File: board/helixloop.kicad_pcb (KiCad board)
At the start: 2 copper layers, 139.8 x 139.8 mm, 357 parts

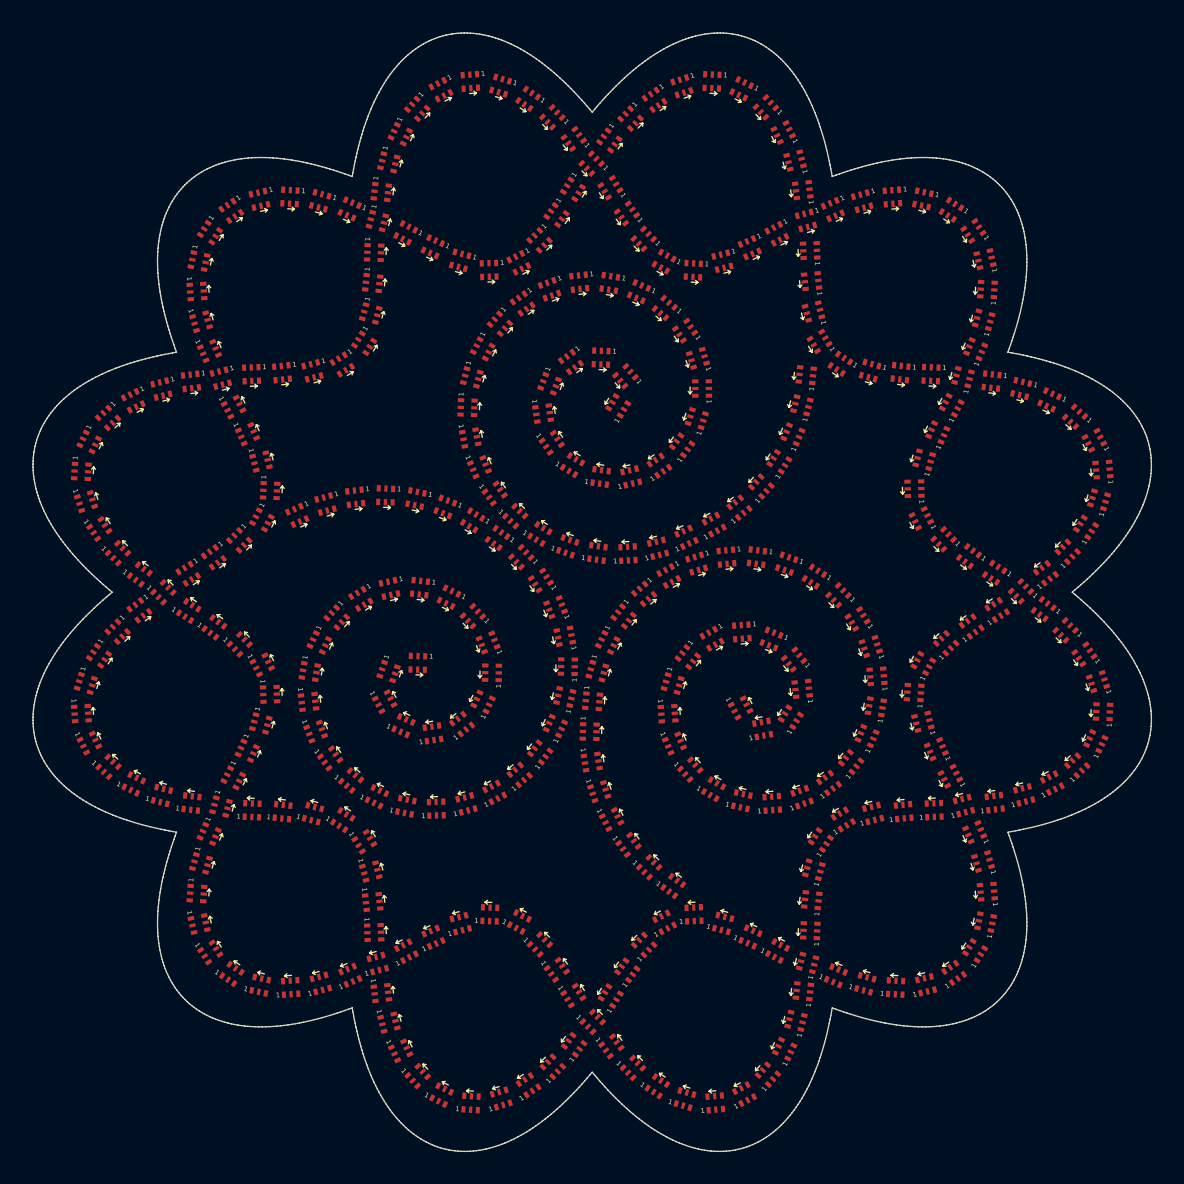
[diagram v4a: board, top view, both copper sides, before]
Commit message: add a spiral drawing created & imported from svg
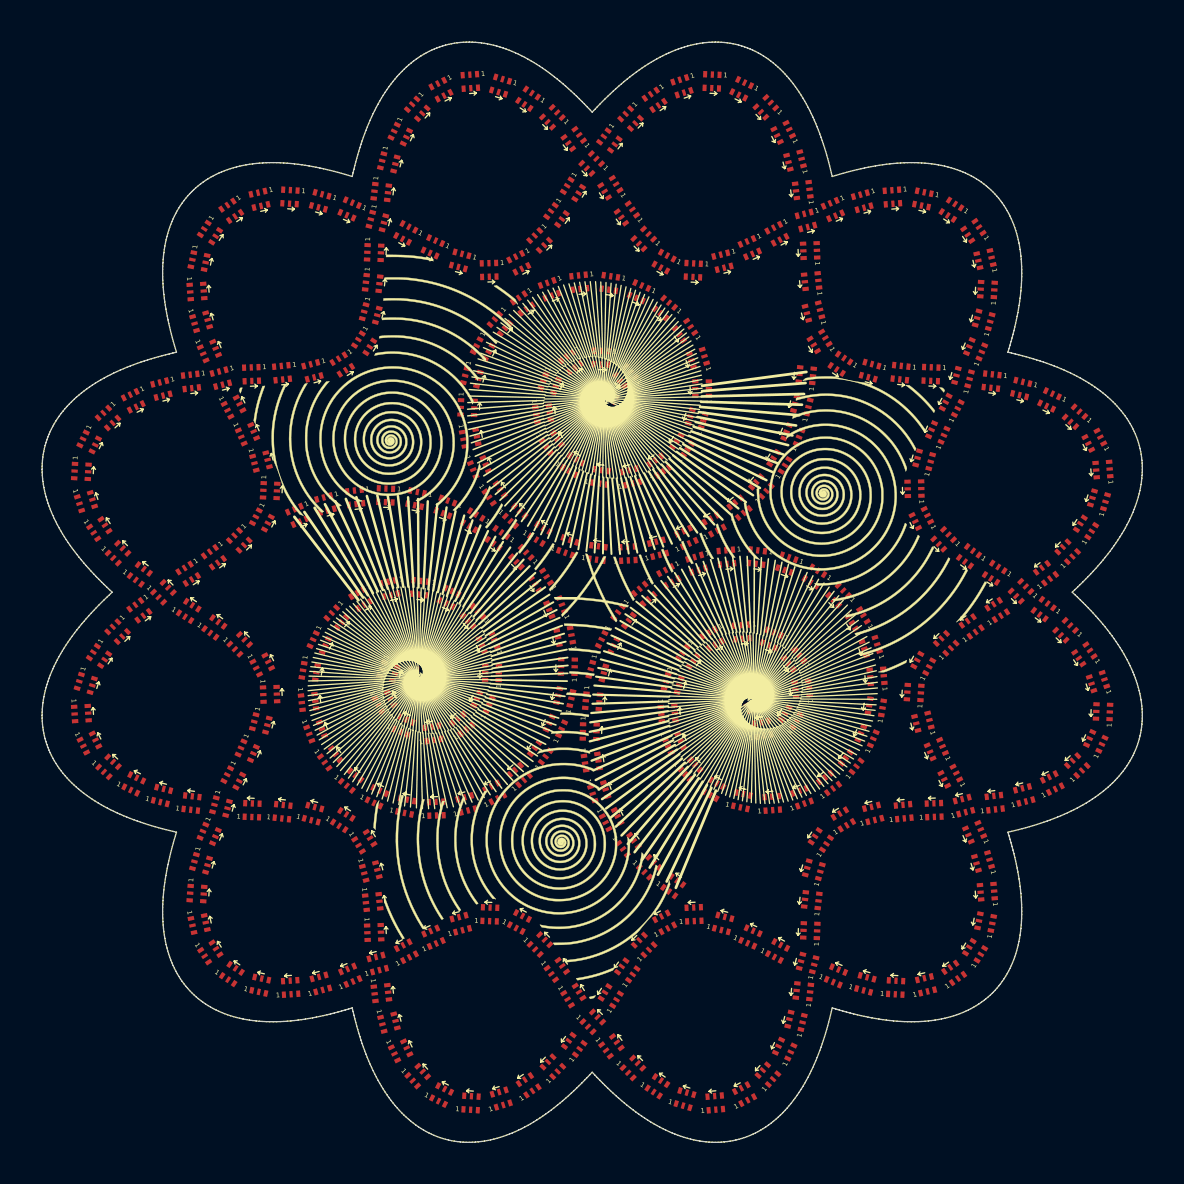
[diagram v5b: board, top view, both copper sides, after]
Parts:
- added spiraldrawing: G***, spiraldrawing, F.SilkS at (100.0, 100.0)
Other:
- board size 139.8 x 139.8 mm -> 137.5 x 137.5 mm

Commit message: extend pixel-spiral line decoration outside the spiral and clip it really nicely along the helix
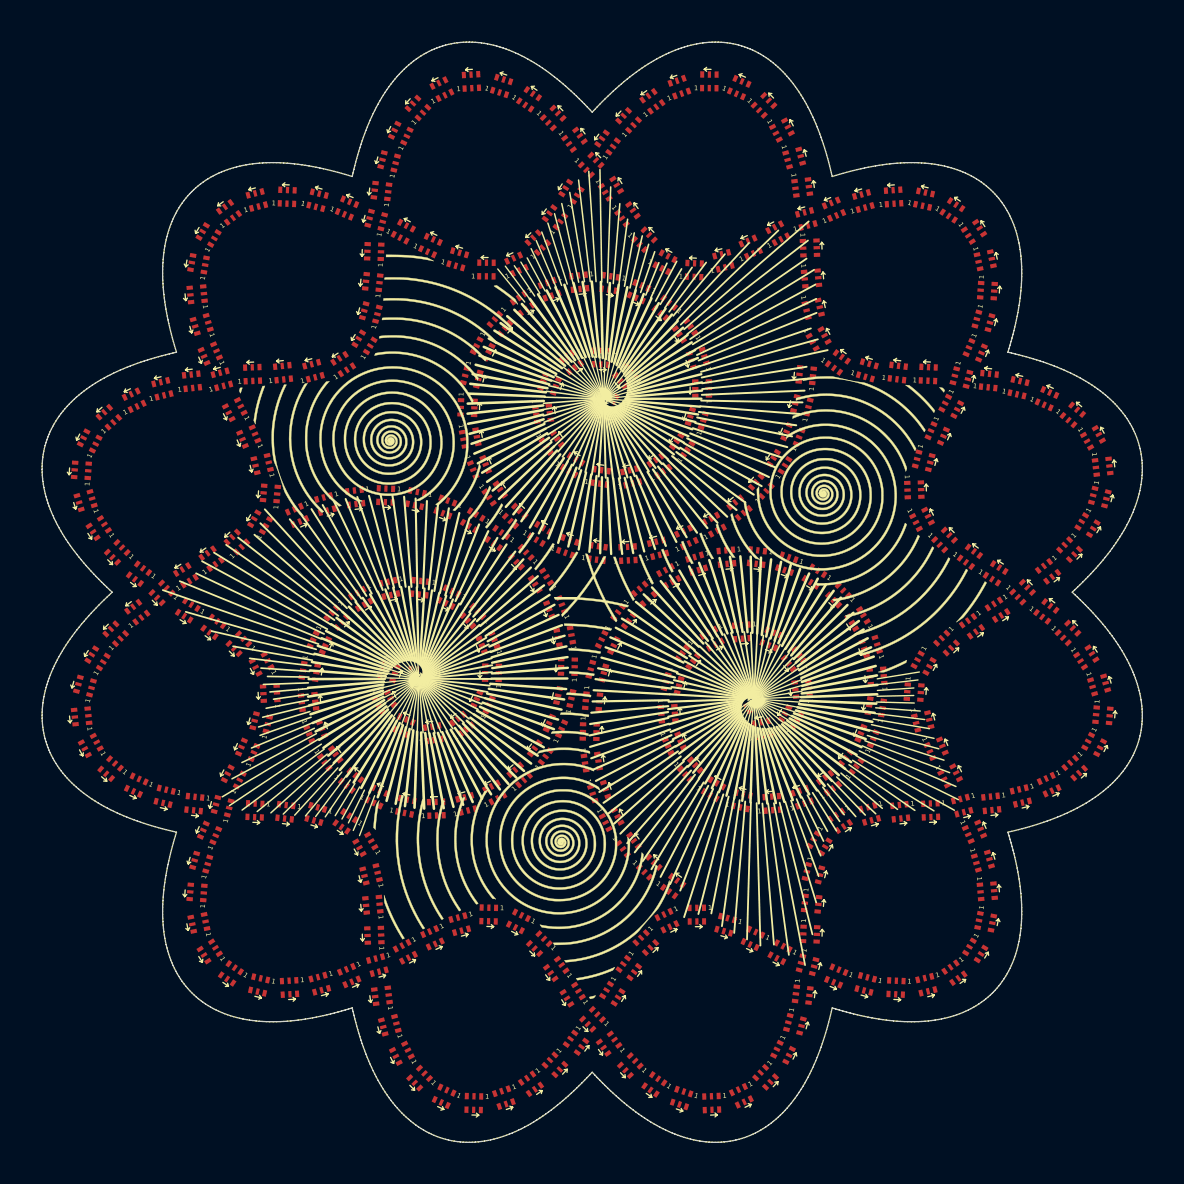
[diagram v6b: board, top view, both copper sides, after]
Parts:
- removed D130, D150, D170, D190, D210, D230: LED-SK9822-EC20, LED-SK9822-EC20
- added D132: LED-SK9822-EC20, LED-SK9822-EC20, F.Cu at (148.8, 133.6)
- added D152: LED-SK9822-EC20, LED-SK9822-EC20, F.Cu at (95.3, 159.1)
- added D172: LED-SK9822-EC20, LED-SK9822-EC20, F.Cu at (46.6, 125.5)
- added D192: LED-SK9822-EC20, LED-SK9822-EC20, F.Cu at (51.2, 66.5)
- added D212: LED-SK9822-EC20, LED-SK9822-EC20, F.Cu at (104.5, 41.0)
- added D232: LED-SK9822-EC20, LED-SK9822-EC20, F.Cu at (153.3, 74.4)
- spiraldrawing: moved to F.Cu
- moved D46 131.2 mm to (54.8, 147.6), turned to -34.2981 degrees
- moved D107 131.2 mm to (147.7, 55.0), turned to 123.458 degrees
- moved D106 131.2 mm to (145.0, 52.3), turned to 146.667 degrees
- moved D47 131.1 mm to (52.2, 144.9), turned to -57.5051 degrees
- moved D45 128.3 mm to (58.4, 149.1), turned to -13.2091 degrees
- moved D108 128.2 mm to (149.1, 58.5), turned to 102.504 degrees
- moved D105 128.1 mm to (141.5, 50.9), turned to 167.581 degrees
- moved D48 128.0 mm to (50.8, 141.3), turned to -78.2818 degrees
- moved D44 123.4 mm to (62.2, 149.4), turned to 3.32799 degrees
- moved D109 123.2 mm to (149.4, 62.3), turned to 86.1578 degrees
- moved D104 123.1 mm to (137.7, 50.6), turned to -176.088 degrees
- moved D49 122.9 mm to (50.6, 137.5), turned to -94.4441 degrees
- moved D43 117.4 mm to (66.0, 148.9), turned to 15.2917 degrees
- moved D110 117.1 mm to (148.9, 66.1), turned to 74.3589 degrees
- moved D103 117.1 mm to (133.9, 51.1), turned to -164.307 degrees
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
